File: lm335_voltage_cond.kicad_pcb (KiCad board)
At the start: 2 copper layers, 35.1 x 25.4 mm, 20 parts, among them K1 OUT, P1 CONN_1, U1 AD8554ARUZ, U2 LM335, p2 pin

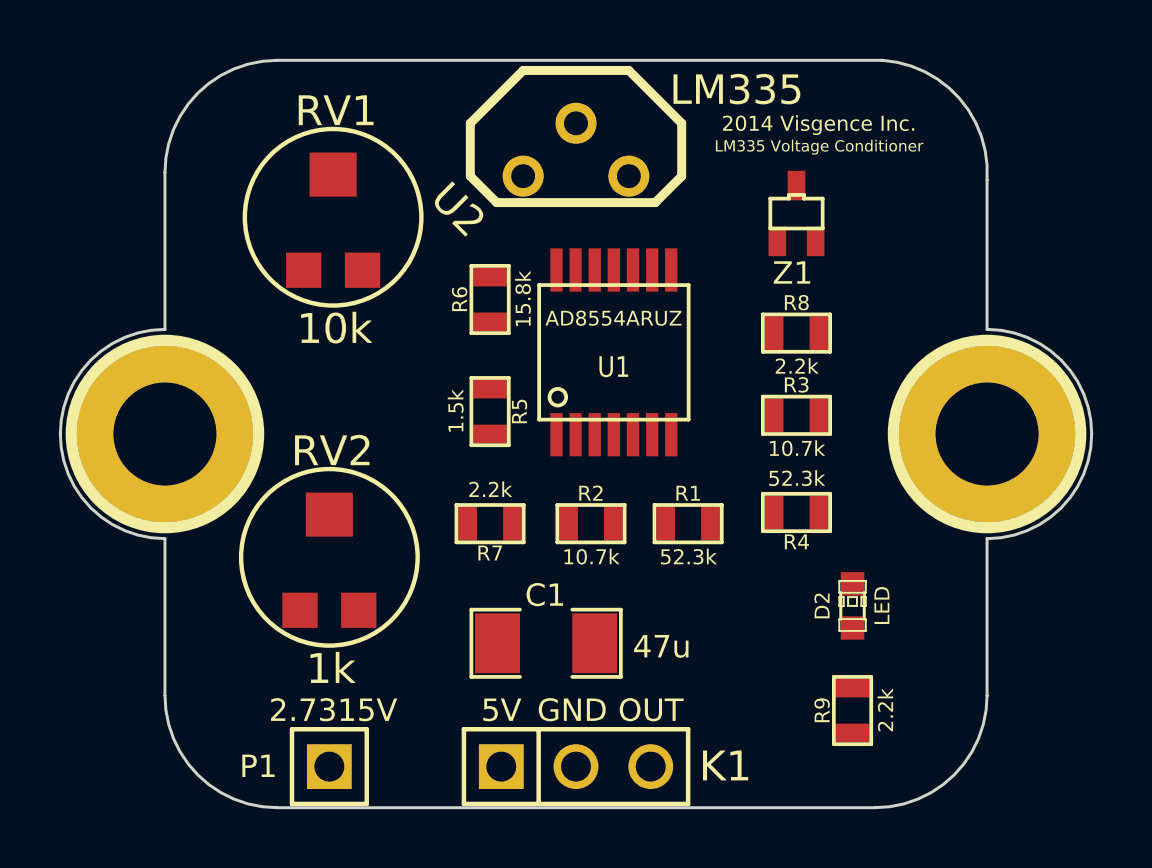
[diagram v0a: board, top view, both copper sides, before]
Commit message: Routed board
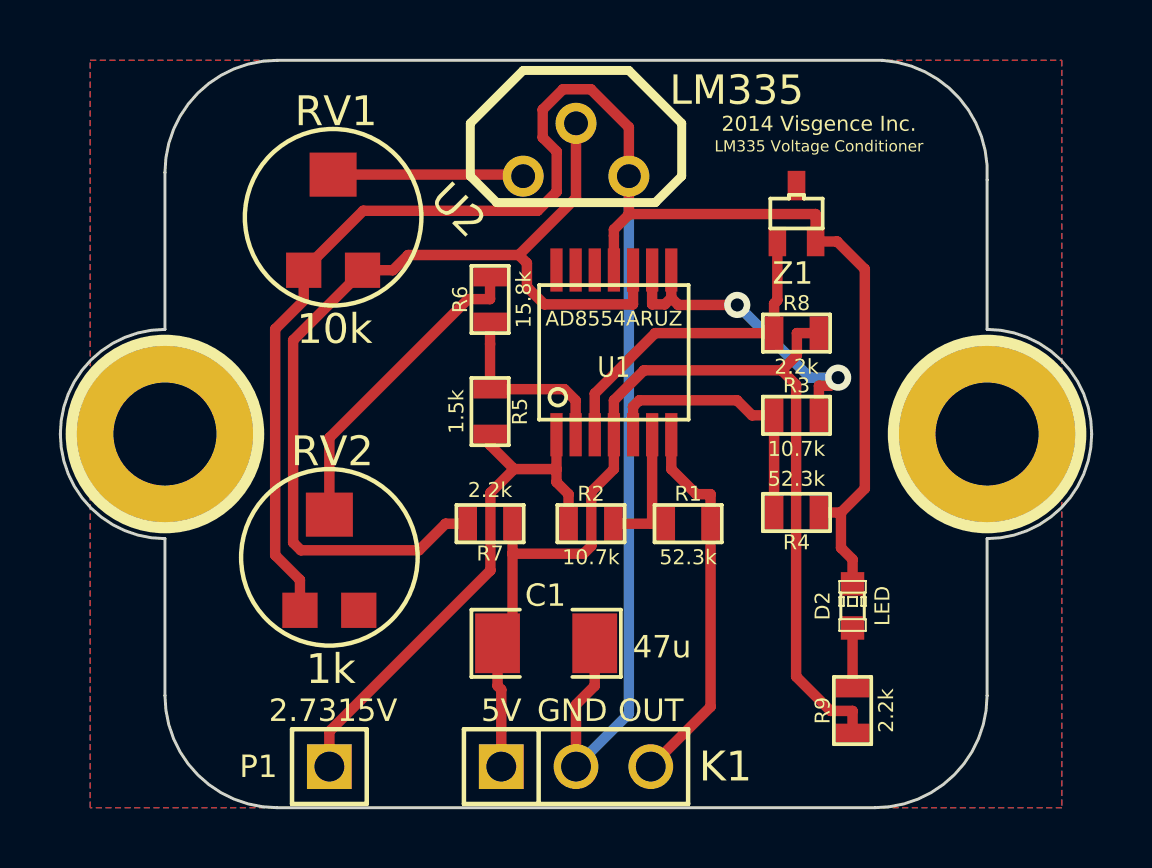
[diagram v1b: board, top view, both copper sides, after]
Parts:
- added G***: LOGO, LOGOMIRROR, B.Cu at (36.6, 42.2)
- renumbered p2 to h1, p2 to h2
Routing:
- net GND: track 0.00 -> 80.4 mm
- net +5V: track 0.00 -> 39.4 mm
- net /TEMP: track 0.00 -> 33.7 mm
- net N-000008: track 0.00 -> 18.9 mm
- net /OUT: track 0.00 -> 13.0 mm
- net N-000006: track 0.00 -> 11.5 mm
- net N-0000016: track 0.00 -> 11.4 mm, vias 0 -> 2
- net N-000003: track 0.00 -> 10.8 mm
- net N-0000018: track 0.00 -> 9.35 mm
- net N-000009: track 0.00 -> 6.52 mm
- net N-000005: track 0.00 -> 6.48 mm
- net N-0000011: track 0.00 -> 4.80 mm
- net N-000007: track 0.00 -> 2.04 mm
- added copper zone on B.Cu, net GND
- added copper zone on F.Cu, net GND
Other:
- net class Default: clearance 0.254 -> 0.2032; trace_width 0.254 -> 0.3556
- rule trace_clearance: 0.254 -> 0.2032
